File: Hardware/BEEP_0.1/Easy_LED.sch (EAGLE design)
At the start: 9 parts, among them IC2 74HC238D

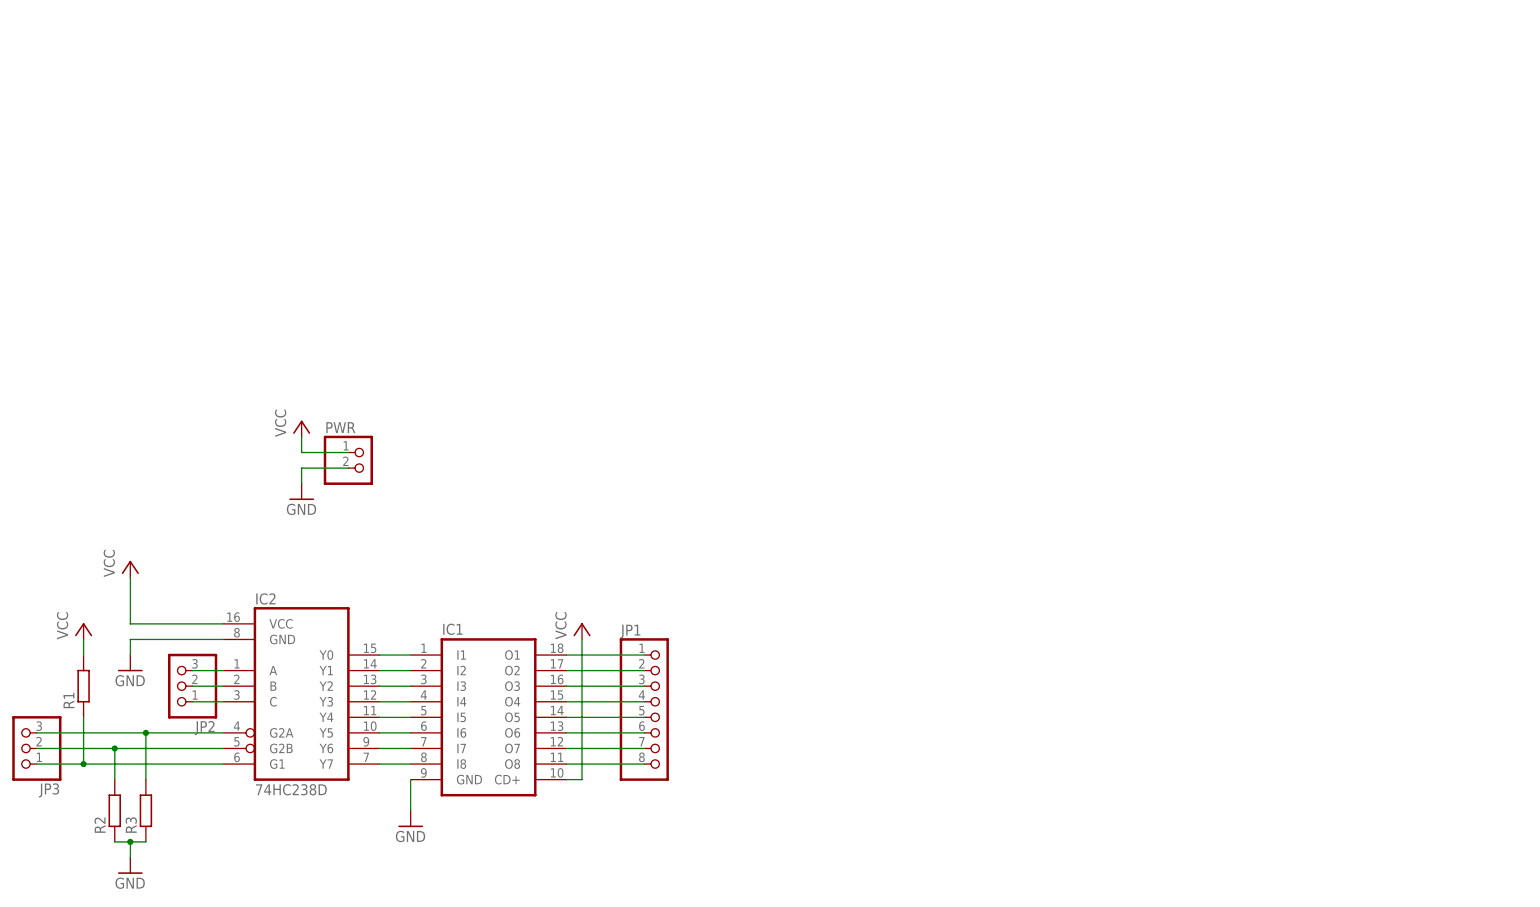
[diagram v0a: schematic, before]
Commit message: Add branding ;) enhance PCBs finish Easy RGB Board add Texas Instruments libray from Element 14 add dxf import ulp for eagle add Script for easy eagle export to pdf for etching minor cleanup
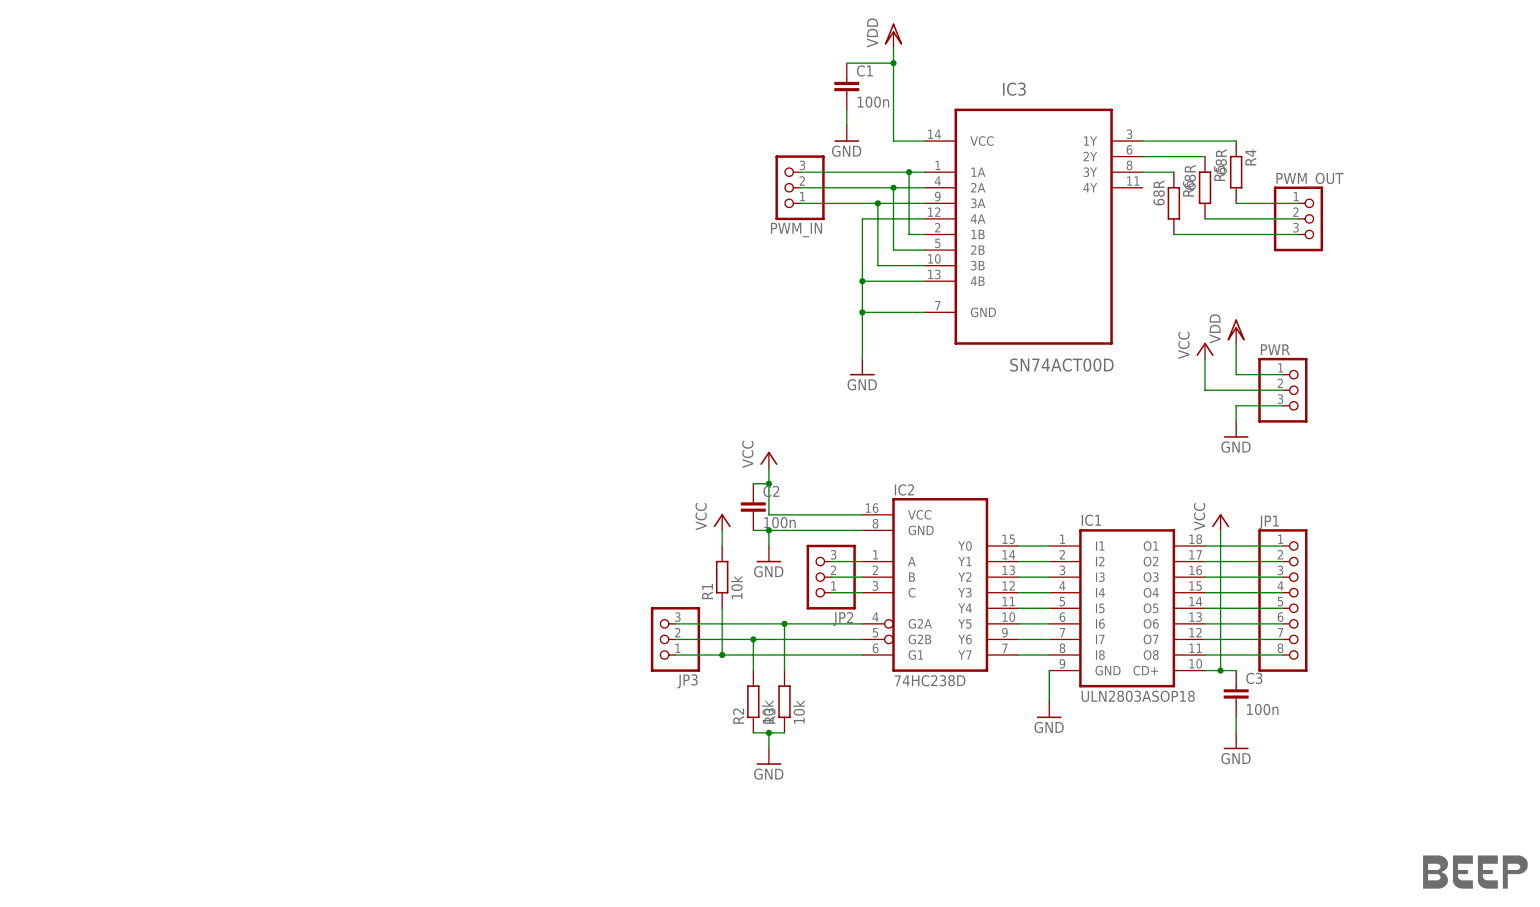
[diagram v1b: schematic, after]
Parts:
- added C1, C2, C3: 100n, rcl:C-EUC0805
- added IC3: SN74ACT00D, Texas Instruments_By_element14_Batch_1:SN74ACT00D
- added PWM_IN, PWM_OUT: (no value), pinhead:PINHD-1X3
- added R4, R5, R6: 68R, rcl:R-EU_M0805
- added U$4: LOGO-COPPER6, Branding:LOGO-COPPER6
- IC1: value (none) -> ULN2803ASOP18
- PWR: device pinhead:PINHD-1X2 -> pinhead:PINHD-1X3
- R1, R2, R3: value (none) -> 10k
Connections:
- new net N$12: IC3.1A, IC3.1B, PWM_IN.3
- new net N$13: IC3.2A, IC3.2B, PWM_IN.2
- new net N$14: IC3.3A, IC3.3B, PWM_IN.1
- new net N$18: PWM_OUT.3, R6.2
- new net N$19: PWM_OUT.2, R5.2
- new net N$20: PWM_OUT.1, R4.2
- new net N$21: IC3.1Y, R4.1
- new net N$25: IC3.2Y, R5.1
- new net N$26: IC3.3Y, R6.1
- new net VDD: C1.1, IC3.VCC, PWR.1
- net GND: now also C1.2, C2.2, C3.2, IC3.4A, IC3.4B, IC3.GND, PWR.3; no longer PWR.2
- net VCC: now also C2.1, C3.1, PWR.2; no longer PWR.1
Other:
- moved on the sheet: IC2, JP1, JP2, JP3, R1, R2, R3
